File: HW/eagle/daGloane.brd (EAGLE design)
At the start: 182.4 x 160.7 mm, 61 parts, among them IC1 MCP1252-33X50, U1 STM32F10XTXU6, X2 USB-MICROB

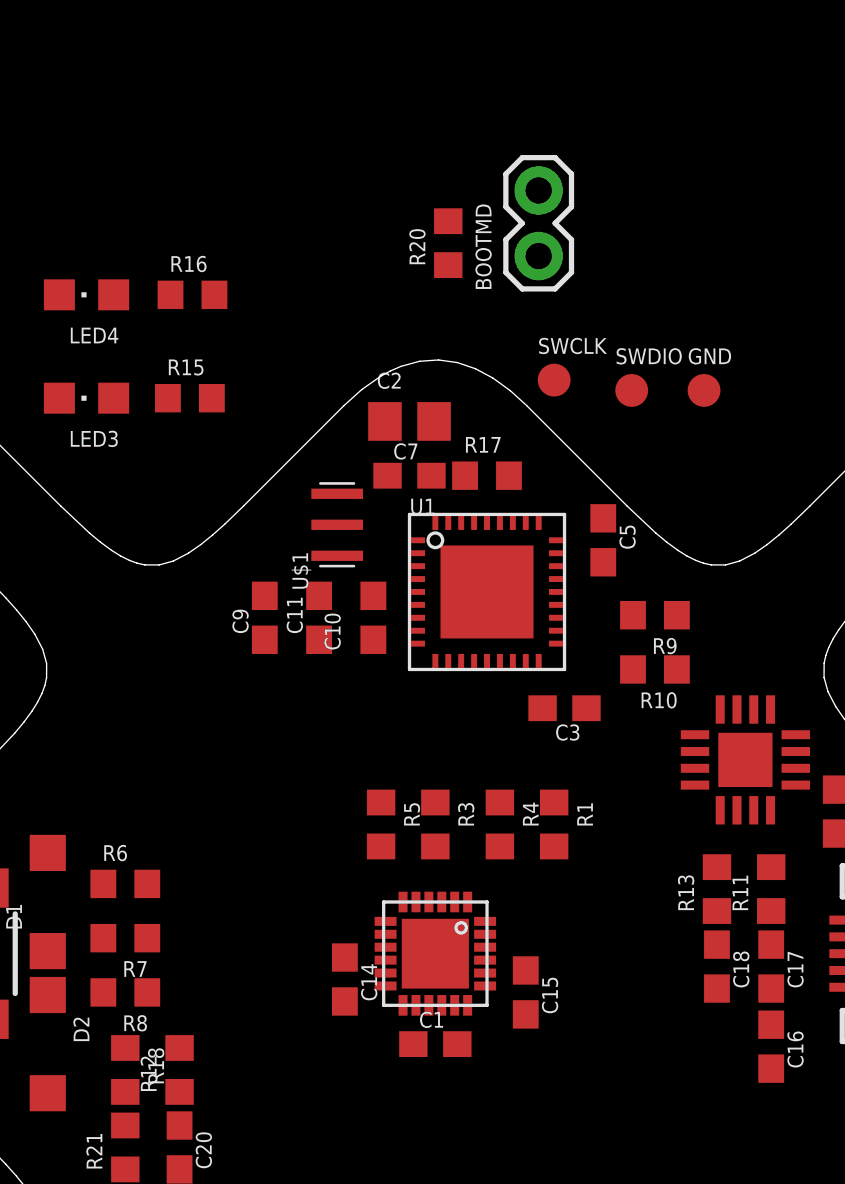
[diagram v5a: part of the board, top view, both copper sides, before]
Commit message: all non standart part replaced by parts found in the daGloane.lbr library
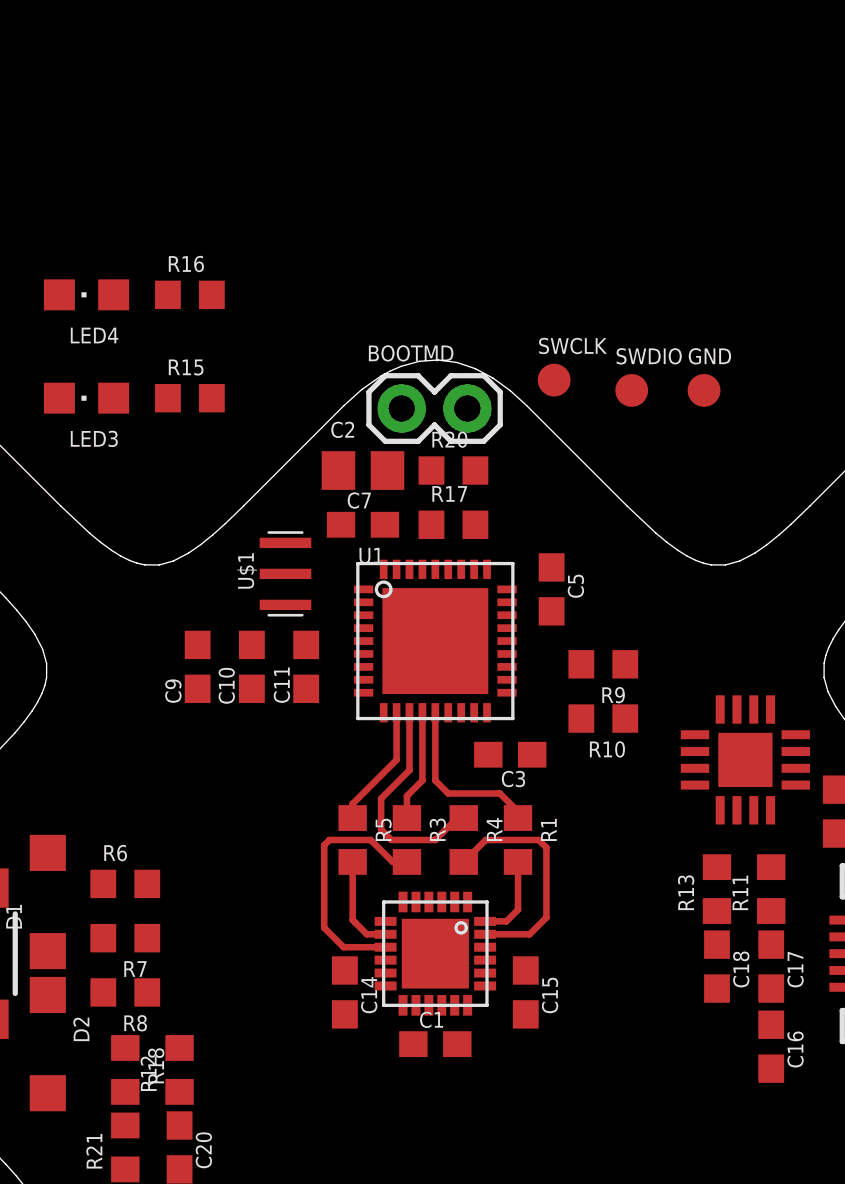
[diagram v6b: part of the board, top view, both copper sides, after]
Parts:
- GND, SWCLK, SWDIO: device bldc_can:TESTPAD_B1,27 -> daGloane:TESTPAD_B1,27
- IC1: device microchip-MCP125x-xxx:MSOP8 -> daGloane:MSOP8
- ON/OFF: device SparkFun-Electromechanical:TACTILE_SWITCH_SMD -> daGloane:TACTILE_SWITCH_SMD
- R15, R16: value 68R -> 150R
- U$1: device canBLC2:MURATA-FILTER_CSTCE__G -> daGloane:MURATA-FILTER_CSTCE__G
- U$2: device LiPo-USB-Charger-v21:SPARKFUN_SOT23-5 -> daGloane:SPARKFUN_SOT23-5
- U$3: device MPU6000:MPU6000 -> daGloane:MPU6000
- U$4: device ftdiftx:SERIAL_QFN4X4-16 -> daGloane:SERIAL_QFN4X4-16
- U1: device stm32:VFQFPN36 -> daGloane:VFQFPN36
- moved R20 8.80 mm to (41.2, 59.2), turned to 0 degrees
- moved BOOTMD 7.93 mm to (39.2, 61.6), turned to 0 degrees
- moved C10 5.07 mm to (33.4, 51.6)
- moved C9 3.22 mm to (31.3, 51.6)
- moved C3 2.77 mm to (43.4, 48.2)
- moved C5 2.76 mm to (45.0, 54.6)
- moved R10 2.76 mm to (47.0, 49.6)
- moved R9 2.76 mm to (47.0, 51.7)
- moved U$1 2.76 mm to (34.7, 55.2)
- moved U1 2.76 mm to (40.5, 52.6)
- moved C2 2.62 mm to (37.7, 59.2)
- moved C7 2.62 mm to (37.7, 57.1)
- moved R17 2.30 mm to (41.2, 57.1)
- moved C11 1.96 mm to (35.5, 51.6)
- moved R1 1.52 mm to (43.7, 44.9)
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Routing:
- net N$18: track 0.00 -> 9.52 mm
- net N$13: track 0.00 -> 9.02 mm
- net SPI1_SCK: track 0.00 -> 8.70 mm
- net SPI1_MOSI: track 0.00 -> 6.57 mm
- net SPI1_CS: track 0.00 -> 4.78 mm
- net SPI1_MISO: track 0.00 -> 4.32 mm
- net N$4: track 0.00 -> 3.75 mm
- net N$19: track 0.00 -> 3.31 mm

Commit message: micro USB b connector added to daGloane lbr
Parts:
- X2: value USB-MICROB -> SPARKFUN-CONNECTORS_USB-MICROB; device SparkFun-Connectors:USB-MICROB -> daGloane:SPARKFUN-CONNECTORS_USB-MICROB
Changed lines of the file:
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@@
 <element name="SWDIO" library="daGloane" package="TESTPAD_B1,27" value="TESTPAD_TPB1,27" x="48.1" y="62.3" smashed="yes">
 <attribute name="NAME" x="47.465" y="63.316" size="0.6096" layer="25" ratio="10"/>
-<attribute name="VALUE" x="47.465" y="61.538" size="0.6096" layer="27"/>
 </element>
 <element name="SWCLK" library="daGloane" package="TESTPAD_B1,27" value="TESTPAD_TPB1,27" x="45.1" y="62.7" smashed="yes">
 <attribute name="NAME" x="44.465" y="63.716" size="0.6096" layer="25" ratio="10"/>
-<attribute name="VALUE" x="44.465" y="61.938" size="0.6096" layer="27"/>
 </element>
 <element name="GND" library="daGloane" package="TESTPAD_B1,27" value="TESTPAD_TPB1,27" x="50.9" y="62.3" smashed="yes">
 <attribute name="NAME" x="50.265" y="63.316" size="0.6096" layer="25" ratio="10"/>
-<attribute name="VALUE" x="50.265" y="61.538" size="0.6096" layer="27"/>
 </element>
 <element name="U$3" library="daGloane" package="MPU6000" value="MPU6000" x="40.5" y="40.5" smashed="yes" rot="R270"/>
@@
 <element name="U$1" library="daGloane" package="MURATA-FILTER_CSTCE__G" value="MURATA-FILTER_CSTCE__G" x="34.7" y="55.2" smashed="yes" rot="R90">
 <attribute name="NAME" x="33.476" y="54.56" size="0.6096" layer="25" rot="R90"/>
-<attribute name="VALUE" x="37.094" y="52.66" size="0.6096" layer="27" rot="R90"/>
 </element>
 <element name="C9" library="rcl" package="C0603" value="100nF" x="31.3" y="51.6" smashed="yes" rot="R90">
@@
 <attribute name="VALUE" x="32.64" y="52.13" size="0.6096" layer="27" rot="R90"/>
 </element>
-<element name="X2" library="SparkFun-Connectors" package="USB-MICROB" value="USB-MICROB" x="59.1" y="40.5" rot="R90"/>
+<element name="X2" library="daGloane" package="SPARKFUN-CONNECTORS_USB-MICROB" value="SPARKFUN-CONNECTORS_USB-MICROB" x="59.1" y="40.5" rot="R90"/>
 </elements>
 <signals>

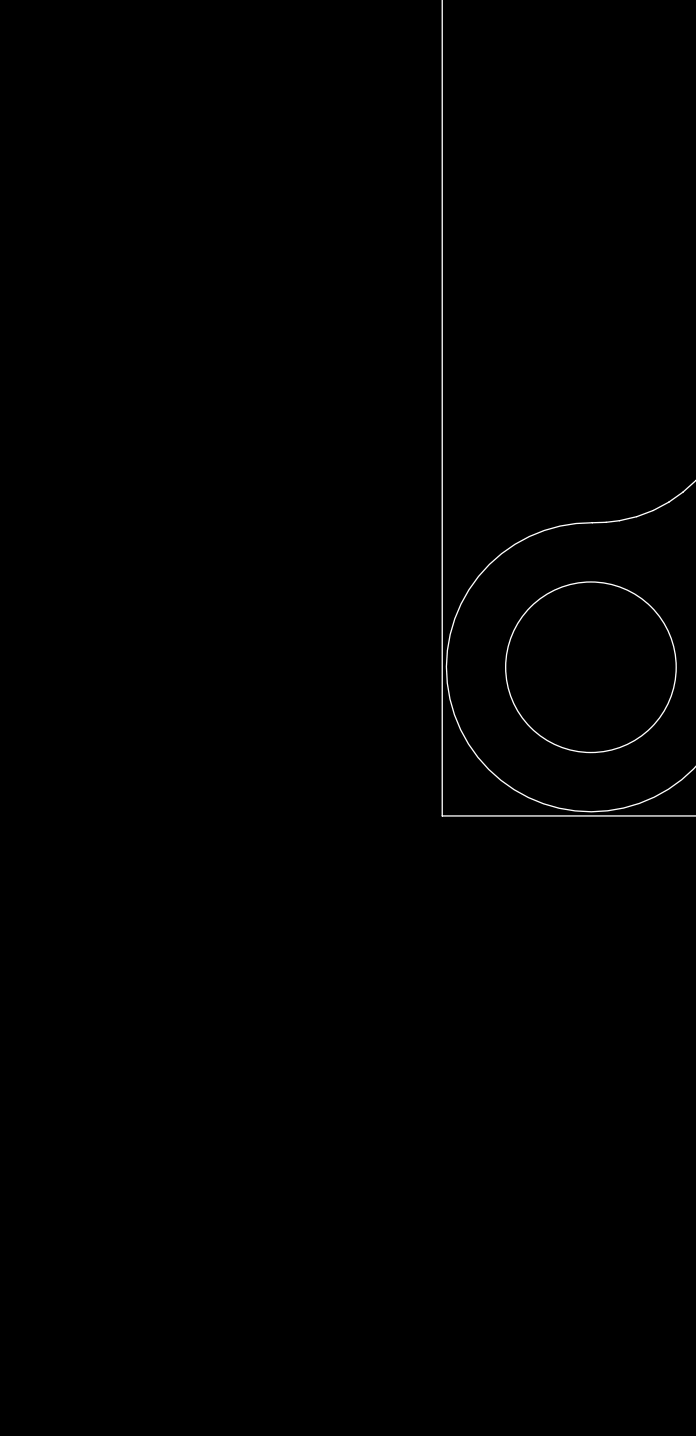
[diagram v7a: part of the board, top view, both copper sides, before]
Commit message: added bluetooth
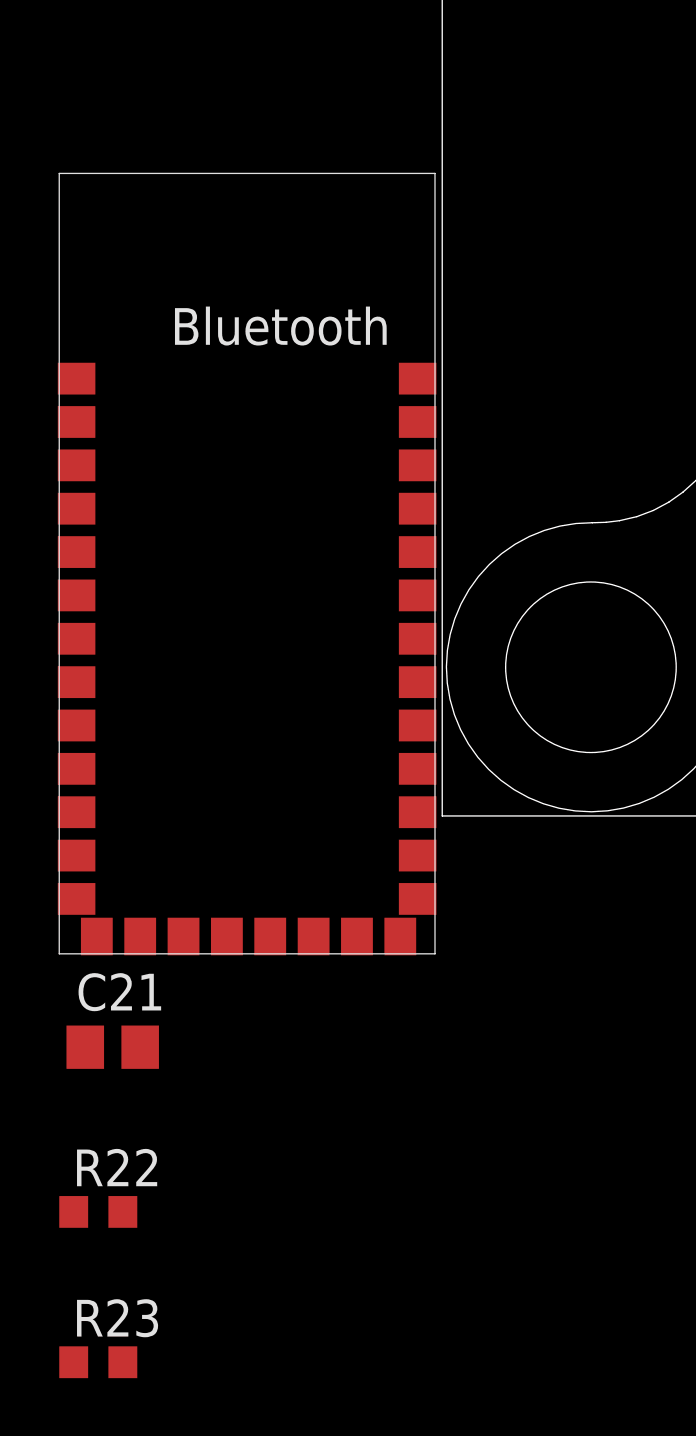
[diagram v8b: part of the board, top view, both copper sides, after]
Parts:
- added C21: 10µF/6.3V, rcl:C0805
- added R22, R23: 1k, rcl:R0603
- added U$5: BLUETOOTH, daGloane:BLUETOOTH
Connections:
- new net N$15: R23.2, U$5.P$2
- new net N$7: R22.2, U$5.P$1
- net GND: now also C21.2, U$5.P$13, U$5.P$14, U$5.P$21, U$5.P$22
- net VCC: now also C21.1, U$5.P$11, U$5.P$12
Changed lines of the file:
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@@
 </element>
 <element name="X2" library="daGloane" package="SPARKFUN-CONNECTORS_USB-MICROB" value="SPARKFUN-CONNECTORS_USB-MICROB" x="59.1" y="40.5" rot="R90"/>
+<element name="U$5" library="daGloane" package="BLUETOOTH" value="BLUETOOTH" x="-6.9" y="10.8"/>
+<element name="C21" library="rcl" package="C0805" value="10µF/6.3V" x="-11.4" y="-8"/>
+<element name="R22" library="rcl" package="R0603" value="1k" x="-11.9" y="-13.7"/>
+<element name="R23" library="rcl" package="R0603" value="1k" x="-11.9" y="-18.9"/>
 </elements>
 <signals>
@@
 <contactref element="U1" pad="5"/>
 <contactref element="X2" pad="GND"/>
+<contactref element="U$5" pad="P$13"/>
+<contactref element="U$5" pad="P$14"/>
+<contactref element="U$5" pad="P$21"/>
+<contactref element="U$5" pad="P$22"/>
+<contactref element="C21" pad="2"/>
 <wire x1="45" y1="53.75" x2="50.9" y2="62.3" width="0" layer="19" extent="1-1"/>
 <wire x1="43.275" y1="54.1" x2="45" y2="53.75" width="0" layer="19" extent="1-1"/>
@@
 <wire x1="40.35" y1="59.2" x2="38.65" y2="59.2" width="0" layer="19" extent="1-1"/>
 <wire x1="37.725" y1="52.6" x2="38.5" y2="55.375" width="0" layer="19" extent="1-1"/>
+<wire x1="35.5" y1="52.45" x2="37.725" y2="52.6" width="0" layer="19" extent="1-1"/>
+<wire x1="33.4" y1="52.45" x2="35.5" y2="52.45" width="0" layer="19" extent="1-1"/>
 <wire x1="31.3" y1="50.75" x2="33.4" y2="52.45" width="0" layer="19" extent="1-1"/>
-<wire x1="34.7" y1="55.2" x2="33.4" y2="52.45" width="0" layer="19" extent="1-1"/>
+<wire x1="34.7" y1="55.2" x2="35.5" y2="52.45" width="0" layer="19" extent="1-1"/>
 <wire x1="41.75" y1="42.5" x2="42.55" y2="48.2" width="0" layer="19" extent="1-1"/>
 <wire x1="41.75" y1="38.5" x2="41.75" y2="42.5" width="0" layer="19" extent="1-1"/>
@@
 <wire x1="25.95" y1="62" x2="34.7" y2="55.2" width="0" layer="19" extent="1-1"/>
 <wire x1="25.95" y1="66" x2="25.95" y2="62" width="0" layer="19" extent="1-1"/>
-<wire x1="33.4" y1="52.45" x2="35.5" y2="52.45" width="0" layer="19" extent="1-1"/>
-<wire x1="35.5" y1="52.45" x2="37.725" y2="52.6" width="0" layer="19" extent="1-1"/>
+<wire x1="-0.85" y1="-2.87" x2="28.5" y2="32.15" width="0" layer="19" extent="1-1"/>
+<wire x1="-1.45" y1="-4.17" x2="-0.85" y2="-2.87" width="0" layer="19" extent="1-1"/>
+<wire x1="-10.45" y1="-8" x2="-1.45" y2="-4.17" width="0" layer="19" extent="1-1"/>
+<wire x1="-11.95" y1="-4.17" x2="-10.45" y2="-8" width="0" layer="19" extent="1-1"/>
+<wire x1="-12.65" y1="-2.87" x2="-11.95" y2="-4.17" width="0" layer="19" extent="1-1"/>
 </signal>
 <signal name="LED1">
@@
 <contactref element="C10" pad="1"/>
 <contactref element="U1" pad="6"/>
+<contactref element="C21" pad="1"/>
+<contactref element="U$5" pad="P$12"/>
+<contactref element="U$5" pad="P$11"/>
 <wire x1="36.75" y1="59.2" x2="39.2" y2="61.6" width="0" layer="19" extent="1-1"/>
 <wire x1="36.85" y1="57.1" x2="36.75" y2="59.2" width="0" layer="19" extent="1-1"/>
 <wire x1="37.725" y1="54.6" x2="36.85" y2="57.1" width="0" layer="19" extent="1-1"/>
 <wire x1="37.725" y1="52.1" x2="37.725" y2="54.6" width="0" layer="19" extent="1-1"/>
+<wire x1="35.5" y1="50.75" x2="37.725" y2="52.1" width="0" layer="19" extent="1-1"/>
 <wire x1="33.4" y1="50.75" x2="35.5" y2="50.75" width="0" layer="19" extent="1-1"/>
 <wire x1="43.275" y1="54.6" x2="37.725" y2="54.6" width="0" layer="19" extent="1-1"/>
@@
 <wire x1="35.45" y1="30.325" x2="39.65" y2="37" width="0" layer="19" extent="1-1"/>
 <wire x1="33.8" y1="29.45" x2="35.45" y2="30.325" width="0" layer="19" extent="1-1"/>
-<wire x1="35.5" y1="50.75" x2="37.725" y2="52.1" width="0" layer="19" extent="1-1"/>
+<wire x1="-12.65" y1="0.13" x2="33.8" y2="29.45" width="0" layer="19" extent="1-1"/>
+<wire x1="-12.65" y1="-1.37" x2="-12.65" y2="0.13" width="0" layer="19" extent="1-1"/>
+<wire x1="-12.35" y1="-8" x2="-12.65" y2="-1.37" width="0" layer="19" extent="1-1"/>
 </signal>
 <signal name="N$11">
@@
 <wire x1="66.35" y1="50.5" x2="67.95" y2="50.5" width="0" layer="19" extent="1-1"/>
 </signal>
+<signal name="N$7">
+<contactref element="U$5" pad="P$1"/>
+<contactref element="R22" pad="2"/>
+<wire x1="-12.65" y1="15.13" x2="-11.05" y2="-13.7" width="0" layer="19" extent="1-1"/>
+</signal>
+<signal name="N$15">
+<contactref element="U$5" pad="P$2"/>
+<contactref element="R23" pad="2"/>
+<wire x1="-12.65" y1="13.63" x2="-11.05" y2="-18.9" width="0" layer="19" extent="1-1"/>
+</signal>
 </signals>
